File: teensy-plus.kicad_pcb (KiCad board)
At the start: 2 copper layers, 30.5 x 39.4 mm, 37 parts, among them J1 Conn_01x03_Male, J10 Conn_01x14, J11 Conn_02x04_Odd_Even, J12 Conn_01x02, J2 Conn_01x03_Male, J3 Conn_01x14_Male, J4 Conn_01x03_Male, J5 Conn_01x05_Male, J6 Conn_01x03_Male, J7 Conn_01x14_Male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

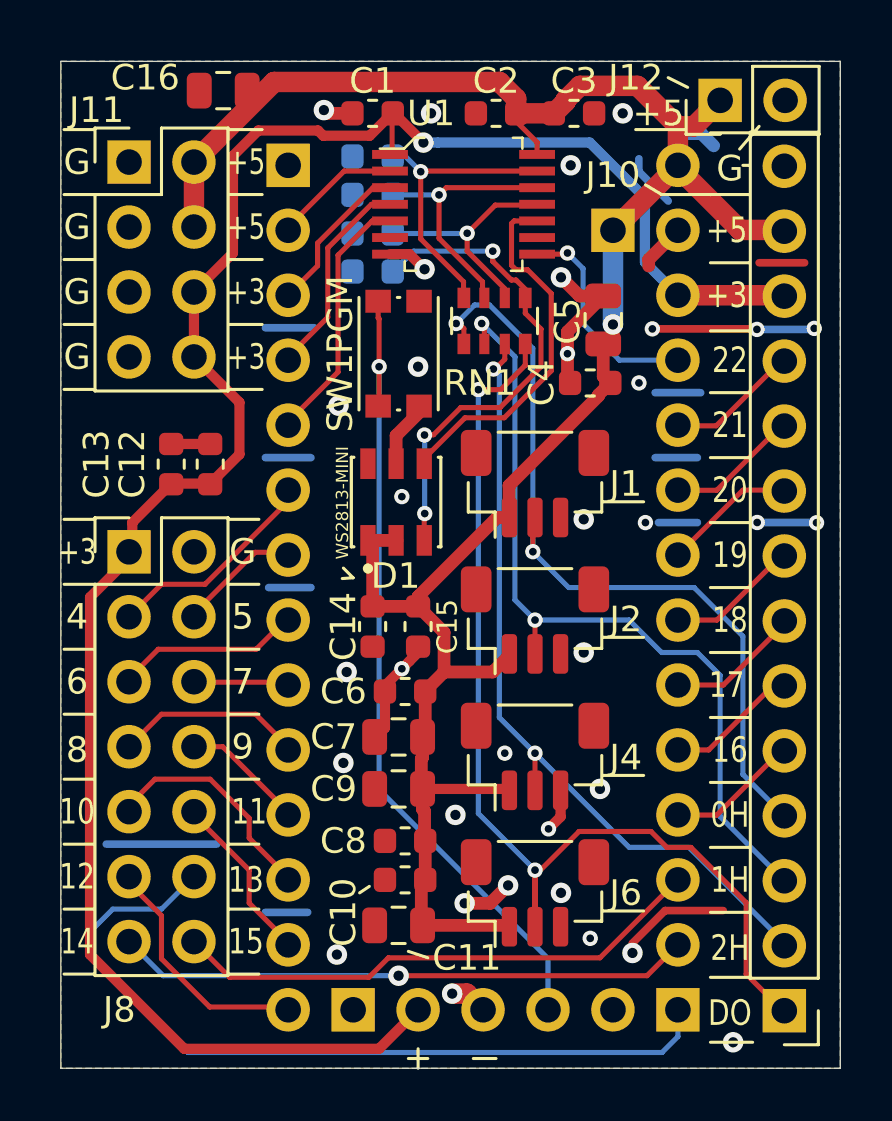
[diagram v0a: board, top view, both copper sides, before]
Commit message: Changed 5V I/O pins to be compatible with FastLED
Also updated the README and added a BOM and other minor cleanups.

Signed-off-by: Aaron Williams <aaron.w2@gmail.com>
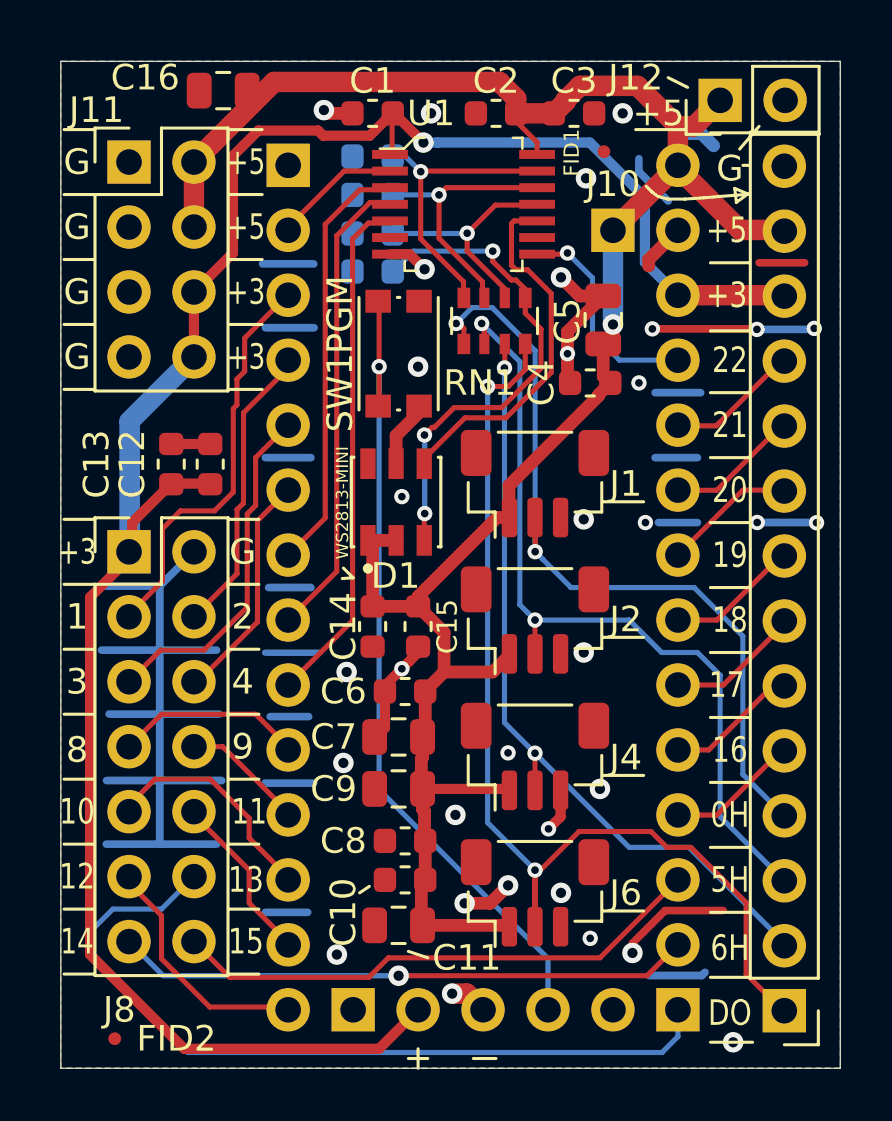
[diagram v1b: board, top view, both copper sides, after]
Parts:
- added FID1: FIDUCIAL_1MM, Fiducial:Fiducial_0.5mm_Mask1mm, F.Cu at (37.7, 34.0)
- added FID2: FIDUCIAL_1MM, Fiducial:Fiducial_0.5mm_Mask1mm, F.Cu at (18.6, 68.7)
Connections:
- net +BATT renamed /VBat
- net /IO1_H renamed /IO5_H
- net /IO1_HR renamed /IO5_HR
- net /IO2_H renamed /IO6_H
- net /IO2_HR renamed /IO6_HR
- J8 pad 3: /IO4 -> /IO1
- J8 pad 4: /IO5 -> /IO2
- J8 pad 5: /IO6 -> /IO3
- J8 pad 6: /IO7 -> /IO4
- U1 pad 3: /IO1 -> /IO5
- U1 pad 4: /IO2 -> /IO6
- U1 pad 5: /IO3 -> /IO7
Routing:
- net GND: track 59.1 -> 96.5 mm, vias 34 -> 33
- net /IO7: track 3.69 -> 20.2 mm
- net /IO5: track 4.68 -> 16.5 mm
- net /IO6: track 7.22 -> 18.6 mm
- net /IO1: track 6.25 -> 15.9 mm
- net /IO3: track 9.92 -> 13.6 mm
- net /IO2: track 8.04 -> 11.5 mm
- net +3V3: track 79.3 -> 82.0 mm
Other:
- board text added: "5H"
- board text added: "6H"
- board text added: "Revision 1.2"
- board text removed: "1H"
- board text removed: "2H"
- board text removed: "Revision 1.1.0"
